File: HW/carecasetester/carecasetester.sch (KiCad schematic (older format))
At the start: 3 parts, among them J4 Conn_01x06_Male, SW1 SW_DIP_x02

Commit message: cc-tester v0.1 gerber filser genereret og 1. print bestilles
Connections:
- net testpoints/TP5: now reaches A1.21 (8)
- net RELAY/Relay_Driver: now reaches A1.29 (6)
- net testpoints/TP4: now reaches A1.30 (7)
- no-connect marks 21 -> 18
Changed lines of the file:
@@
 $Descr A4 11693 8268
 encoding utf-8
-Sheet 1 5
+Sheet 1 6
 Title ""
 Date ""
@@
 F5 "D4" I R 3400 2700 50
 F6 "D5" I R 3400 2775 50
-$EndSheet
-$Sheet
-S 7750 3100 700  375
+F7 "RELAY" I R 3400 2850 50
+$EndSheet
+$Sheet
+S 4150 3800 700  375
 U 5E3DBE35
 F0 "testpoints" 50
 F1 "testpoints.sch" 50
+F2 "TP4" I R 4850 3900 50
+F3 "TP5" I R 4850 4000 50
 $EndSheet
 Wire Wire Line
@@
 NoConn ~ 5275 2800
 NoConn ~ 5275 2900
-NoConn ~ 5275 3500
-NoConn ~ 5275 3600
-NoConn ~ 5275 3700
 NoConn ~ 5275 3800
 Wire Wire Line
@@
 Wire Wire Line
 	6125 2275 6125 1800
+$Sheet
+S 2575 3450 825  600
+U 5E3E43C1
+F0 "RELAY" 50
+F1 "relay.sch" 50
+F2 "Relay_Driver" I R 3400 3750 50
+F3 "RELAY" I R 3400 3575 50
+$EndSheet
+Wire Wire Line
+	3400 3575 3575 3575
+Wire Wire Line
+	3575 3575 3575 2850
+Wire Wire Line
+	3575 2850 3400 2850
+Wire Wire Line
+	3400 3750 3750 3750
+Wire Wire Line
+	3750 3750 3750 3500
+Wire Wire Line
+	3750 3500 5275 3500
+Wire Wire Line
+	4850 3900 4950 3900
+Wire Wire Line
+	4950 3900 4950 3600
+Wire Wire Line
+	4950 3600 5275 3600
+Wire Wire Line
+	4850 4000 5075 4000
+Wire Wire Line
+	5075 4000 5075 3700
+Wire Wire Line
+	5075 3700 5275 3700
 $EndSCHEMATC

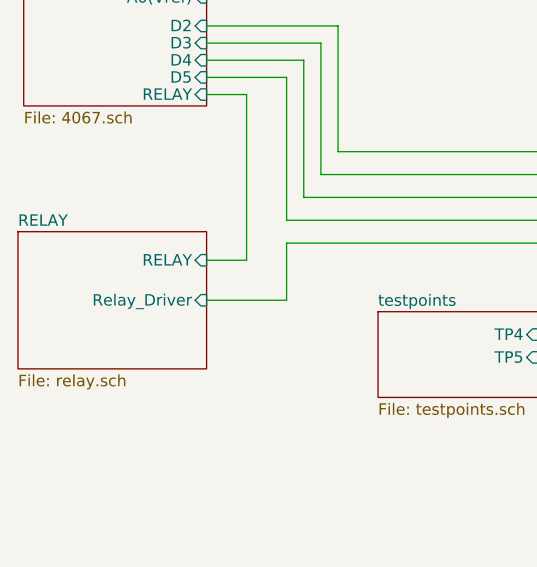
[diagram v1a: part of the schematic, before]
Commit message: Relay sheet filled and all pins matched.
starting changes made to pcb to fit schematic to the new pcb
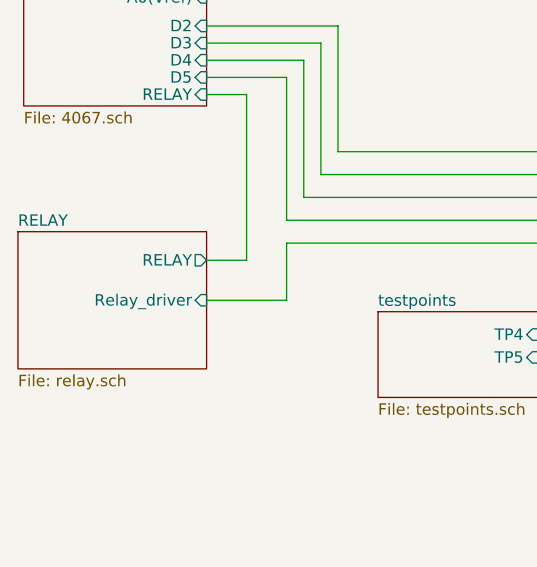
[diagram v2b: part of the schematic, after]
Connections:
- net RELAY/Relay_Driver renamed RELAY/Relay_driver
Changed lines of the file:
@@
 F0 "RELAY" 50
 F1 "relay.sch" 50
-F2 "Relay_Driver" I R 3400 3750 50
-F3 "RELAY" I R 3400 3575 50
+F2 "Relay_driver" I R 3400 3750 50
+F3 "RELAY" O R 3400 3575 50
 $EndSheet
 Wire Wire Line

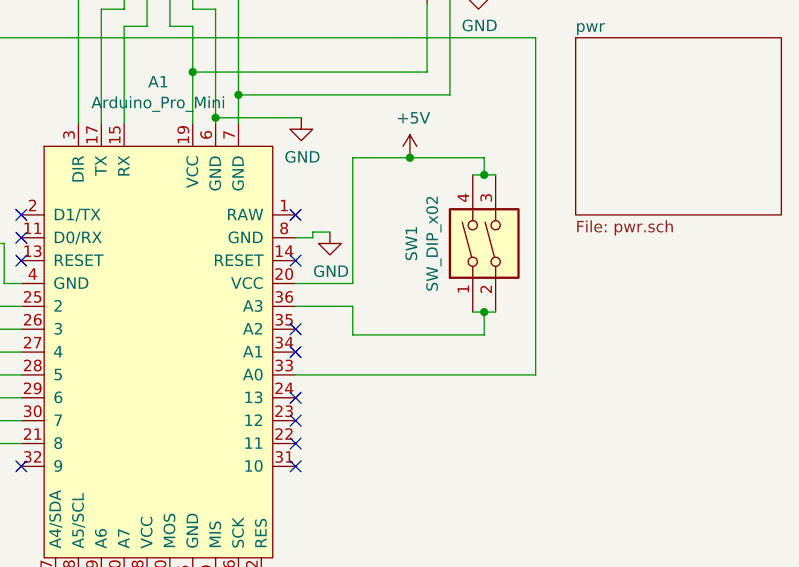
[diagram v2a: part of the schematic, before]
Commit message: First try to fit schematic to pcb (not imported footprints to pcb yet)
Schematic: All known components has gotten an updated footprint
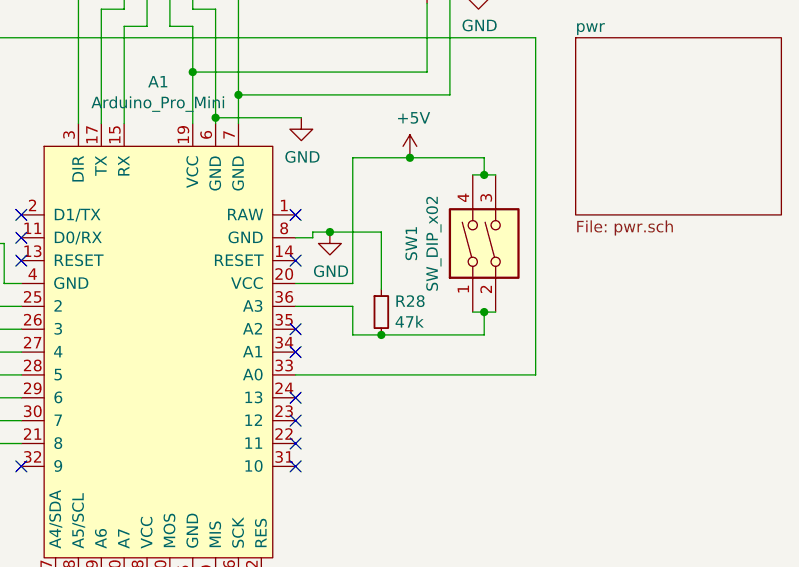
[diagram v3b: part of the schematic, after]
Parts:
- added R28: 47k, Resistor_SMD:R_0603_1608Metric_Pad1.05x0.95mm_HandSolder, symbol Device:R_Small
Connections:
- net GND: now also R28.1
- net at A1.36 (A3), SW1.1, SW1.2: now also R28.2
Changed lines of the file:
@@
 	6725 3100 6725 3225
 Wire Wire Line
-	6725 3225 7300 3225
+	6725 3225 6850 3225
 Wire Wire Line
 	7300 3225 7300 3125
@@
 Wire Wire Line
 	5075 3700 5275 3700
+$Comp
+L Device:R_Small R28
+U 1 1 5E870DAA
+P 6850 3125
+F 0 "R28" H 6909 3171 50  0000 L CNN
+F 1 "47k" H 6909 3080 50  0000 L CNN
+F 2 "Resistor_SMD:R_0603_1608Metric_Pad1.05x0.95mm_HandSolder" H 6850 3125 50  0001 C CNN
+F 3 "~" H 6850 3125 50  0001 C CNN
+	1    6850 3125
+	1    0    0    -1
+$EndComp
+Connection ~ 6850 3225
+Wire Wire Line
+	6850 3225 7300 3225
+Wire Wire Line
+	6850 3025 6850 2775
+Wire Wire Line
+	6850 2775 6625 2775
+Connection ~ 6625 2775
 $EndSCHEMATC

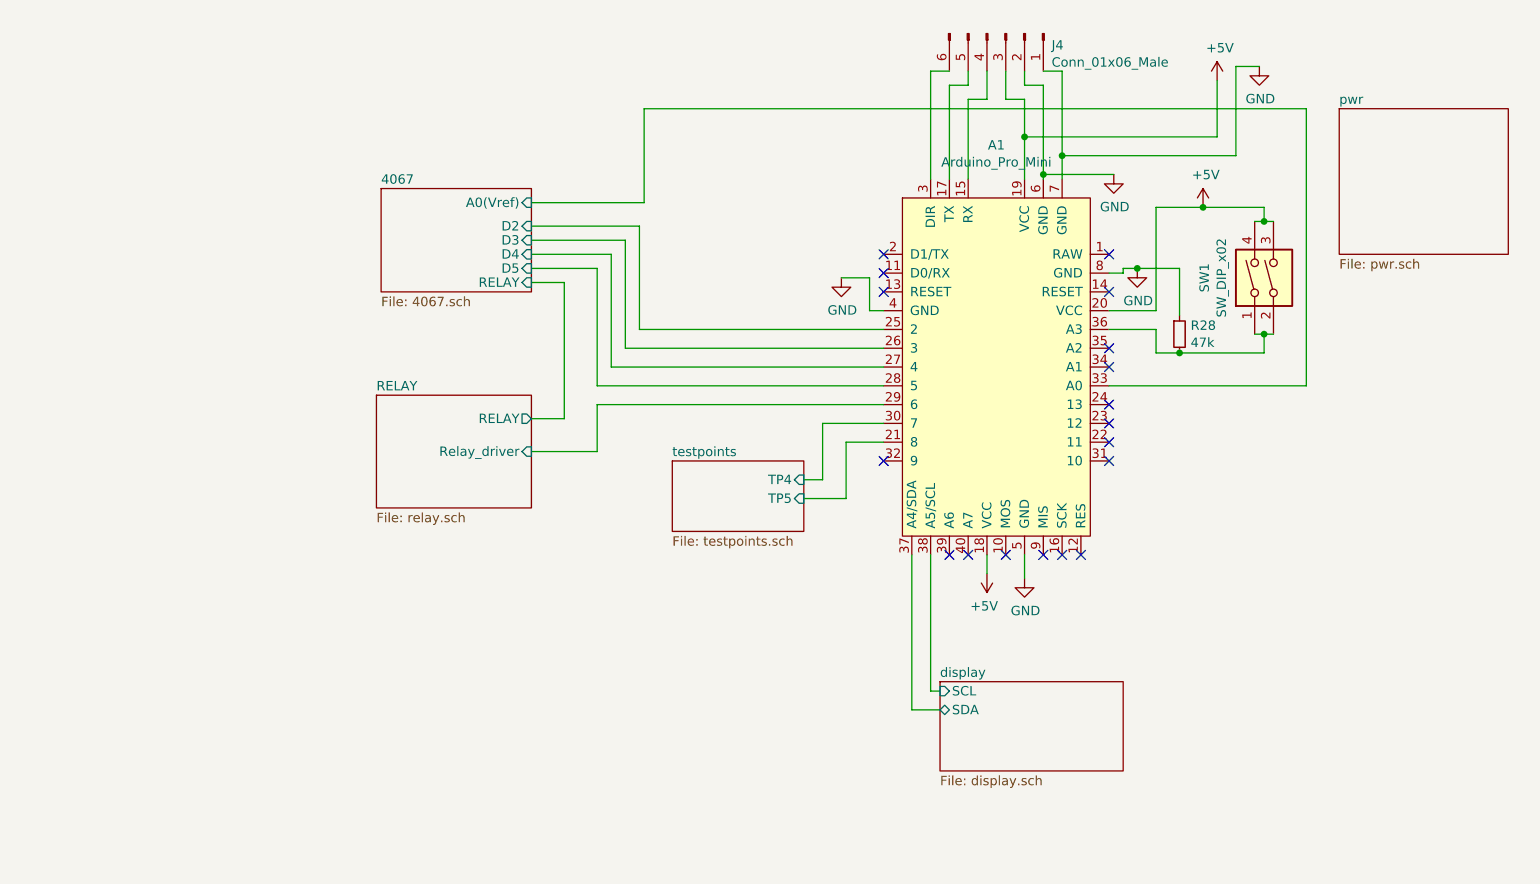
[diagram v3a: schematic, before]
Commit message: Gerbers and drillfiles made and ready to order
edge cuts file renamed to GML instaid of GM1
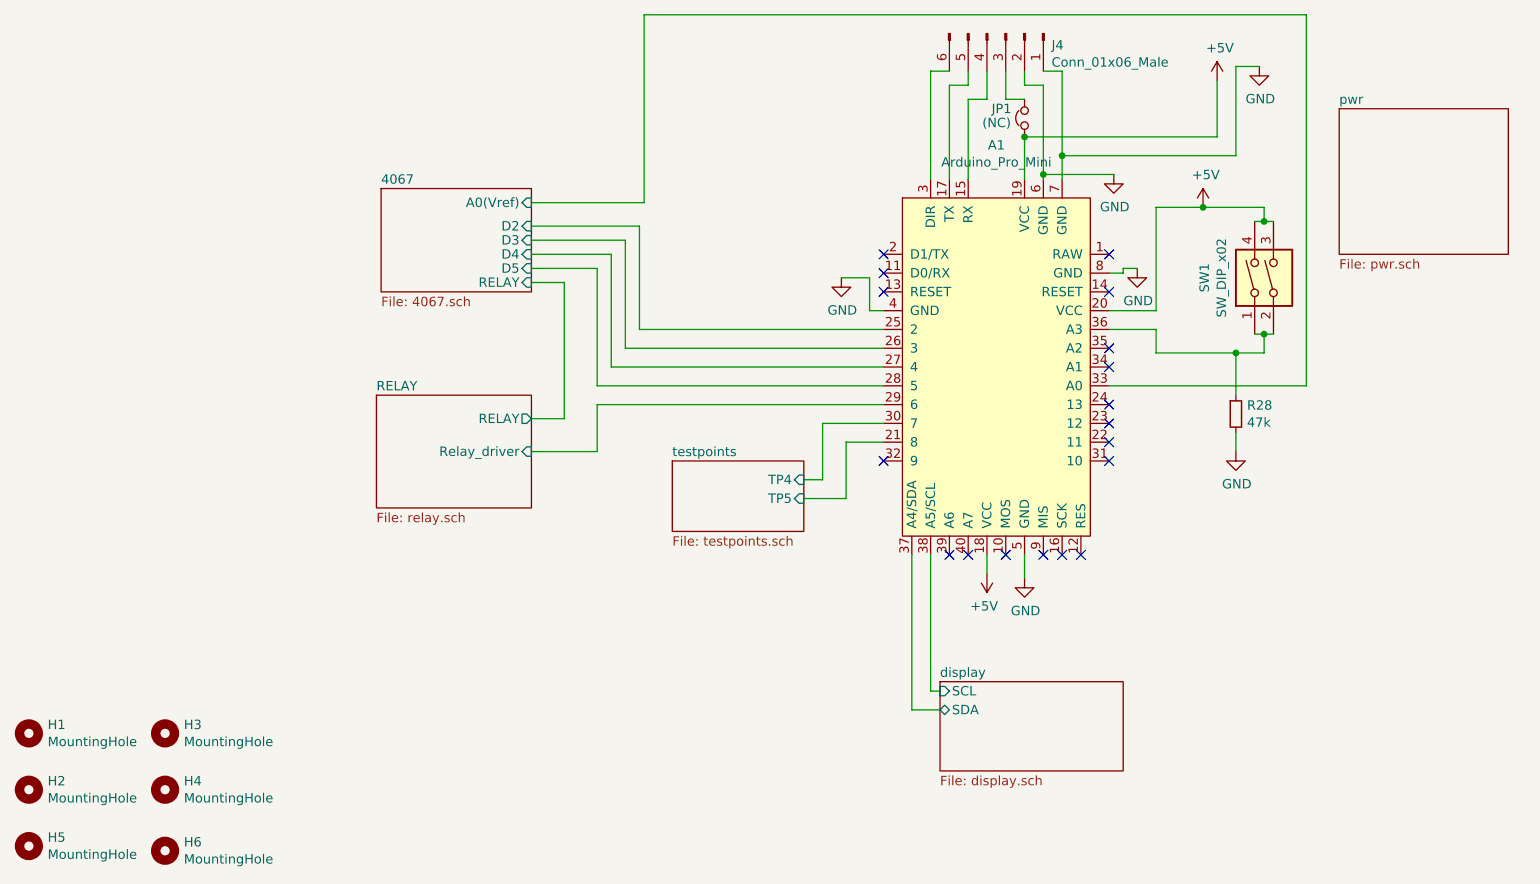
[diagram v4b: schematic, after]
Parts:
- added H1, H2, H3, H4, H5, H6: MountingHole, MountingHole:MountingHole_3.2mm_M3_ISO14580_Pad, symbol Mechanical:MountingHole
- added JP1: (NC), MM:Jumper_P2.54_Vertical_THT, symbol Device:Jumper_NC_Small
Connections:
- net +5V: now also JP1.1; no longer J4.3 (Pin_3)
- net GND: now also R28.2; no longer R28.1
- net at A1.36 (A3), SW1.1, SW1.2: now also R28.1; no longer R28.2
- new net: J4.3 (Pin_3), JP1.2
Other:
- moved on the sheet: R28
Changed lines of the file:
@@
 	3400 2425 4000 2425
 Wire Wire Line
-	4000 2425 4000 1925
-Wire Wire Line
-	7525 1925 7525 3400
+	4000 2425 4000 1425
+Wire Wire Line
+	7525 1425 7525 3400
 Wire Wire Line
 	7525 3400 6475 3400
@@
 	6725 3100 6725 3225
 Wire Wire Line
-	6725 3225 6850 3225
-Wire Wire Line
 	7300 3225 7300 3125
 Connection ~ 7300 3125
@@
 	6475 3100 6725 3100
 Wire Wire Line
-	4000 1925 7525 1925
+	4000 1425 7525 1425
 $Comp
 L Connector:Conn_01x06_Male J4
@@
 	6025 2300 6025 2075
 Wire Wire Line
-	6025 1875 5925 1875
-Wire Wire Line
-	5925 1875 5925 1725
-Wire Wire Line
 	6125 2300 6125 2275
 Wire Wire Line
@@
 Wire Wire Line
 	6225 1725 6125 1725
-Connection ~ 6025 2075
 NoConn ~ 5625 4300
 NoConn ~ 5725 4300
@@
 	1    0    0    -1
 $EndComp
-Wire Wire Line
-	6025 1875 6025 2075
 $Comp
 L power:+5V #PWR0110
@@
 L Device:R_Small R28
 U 1 1 5E870DAA
-P 6850 3125
-F 0 "R28" H 6909 3171 50  0000 L CNN
-F 1 "47k" H 6909 3080 50  0000 L CNN
-F 2 "Resistor_SMD:R_0603_1608Metric_Pad1.05x0.95mm_HandSolder" H 6850 3125 50  0001 C CNN
-F 3 "~" H 6850 3125 50  0001 C CNN
-	1    6850 3125
-	1    0    0    -1
-$EndComp
-Connection ~ 6850 3225
-Wire Wire Line
-	6850 3225 7300 3225
-Wire Wire Line
-	6850 3025 6850 2775
-Wire Wire Line
-	6850 2775 6625 2775
-Connection ~ 6625 2775
+P 7150 3550
+F 0 "R28" H 7209 3596 50  0000 L CNN
+F 1 "47k" H 7209 3505 50  0000 L CNN
+F 2 "Resistor_SMD:R_0603_1608Metric_Pad1.05x0.95mm_HandSolder" H 7150 3550 50  0001 C CNN
+F 3 "~" H 7150 3550 50  0001 C CNN
+	1    7150 3550
+	1    0    0    -1
+$EndComp
+$Comp
+L Mechanical:MountingHole H3
+U 1 1 5E86F871
+P 1450 5250
+F 0 "H3" H 1550 5296 50  0000 L CNN
+F 1 "MountingHole" H 1550 5205 50  0000 L CNN
+F 2 "MountingHole:MountingHole_3.2mm_M3_ISO14580_Pad" H 1450 5250 50  0001 C CNN
+F 3 "~" H 1450 5250 50  0001 C CNN
+	1    1450 5250
+	1    0    0    -1
+$EndComp
+$Comp
+L Mechanical:MountingHole H4
+U 1 1 5E870C6C
+P 1450 5550
+F 0 "H4" H 1550 5596 50  0000 L CNN
+F 1 "MountingHole" H 1550 5505 50  0000 L CNN
+F 2 "MountingHole:MountingHole_3.2mm_M3_ISO14580_Pad" H 1450 5550 50  0001 C CNN
+F 3 "~" H 1450 5550 50  0001 C CNN
+	1    1450 5550
+	1    0    0    -1
+$EndComp
+$Comp
+L Mechanical:MountingHole H1
+U 1 1 5E872C20
+P 725 5250
+F 0 "H1" H 825 5296 50  0000 L CNN
+F 1 "MountingHole" H 825 5205 50  0000 L CNN
+F 2 "MountingHole:MountingHole_3.2mm_M3_ISO14580_Pad" H 725 5250 50  0001 C CNN
+F 3 "~" H 725 5250 50  0001 C CNN
+	1    725  5250
+	1    0    0    -1
+$EndComp
+$Comp
+L Mechanical:MountingHole H2
+U 1 1 5E874A9F
+P 725 5550
+F 0 "H2" H 825 5596 50  0000 L CNN
+F 1 "MountingHole" H 825 5505 50  0000 L CNN
+F 2 "MountingHole:MountingHole_3.2mm_M3_ISO14580_Pad" H 725 5550 50  0001 C CNN
+F 3 "~" H 725 5550 50  0001 C CNN
+	1    725  5550
+	1    0    0    -1
+$EndComp
+$Comp
+L Mechanical:MountingHole H6
+U 1 1 5E877F41
+P 1450 5875
+F 0 "H6" H 1550 5921 50  0000 L CNN
+F 1 "MountingHole" H 1550 5830 50  0000 L CNN
+F 2 "MountingHole:MountingHole_3.2mm_M3_ISO14580_Pad" H 1450 5875 50  0001 C CNN
+F 3 "~" H 1450 5875 50  0001 C CNN
+	1    1450 5875
+	1    0    0    -1
+$EndComp
+$Comp
+L Mechanical:MountingHole H5
+U 1 1 5E877F47
+P 725 5850
+F 0 "H5" H 825 5896 50  0000 L CNN
+F 1 "MountingHole" H 825 5805 50  0000 L CNN
+F 2 "MountingHole:MountingHole_3.2mm_M3_ISO14580_Pad" H 725 5850 50  0001 C CNN
+F 3 "~" H 725 5850 50  0001 C CNN
+	1    725  5850
+	1    0    0    -1
+$EndComp
+$Comp
+L power:GND #PWR07
+U 1 1 5E872E95
+P 7150 3750
+F 0 "#PWR07" H 7150 3500 50  0001 C CNN
+F 1 "GND" H 7155 3577 50  0000 C CNN
+F 2 "" H 7150 3750 50  0001 C CNN
+F 3 "" H 7150 3750 50  0001 C CNN
+	1    7150 3750
+	1    0    0    -1
+$EndComp
+Wire Wire Line
+	6725 3225 7150 3225
+Wire Wire Line
+	7150 3750 7150 3650
+Wire Wire Line
+	7150 3450 7150 3225
+Connection ~ 7150 3225
+Wire Wire Line
+	7150 3225 7300 3225
+$Comp
+L Device:Jumper_NC_Small JP1
+U 1 1 5E88542A
+P 6025 1975
+F 0 "JP1" V 6075 2150 50  0000 R CNN
+F 1 "(NC)" V 6000 2200 50  0000 R CNN
+F 2 "MM:Jumper_P2.54_Vertical_THT" H 6025 1975 50  0001 C CNN
+F 3 "~" H 6025 1975 50  0001 C CNN
+	1    6025 1975
+	0    -1   -1   0
+$EndComp
+Connection ~ 6025 2075
+Wire Wire Line
+	6025 1875 5925 1875
+Wire Wire Line
+	5925 1875 5925 1725
 $EndSCHEMATC

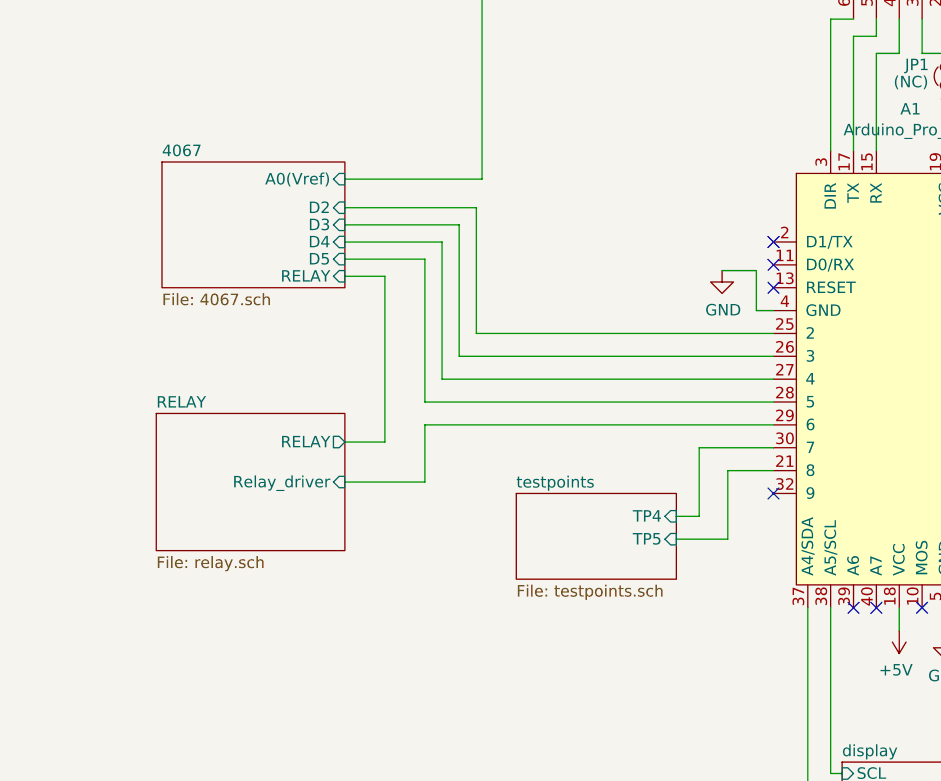
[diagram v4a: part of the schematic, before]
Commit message: V0.22 gerbers
2nd relay added and all should now be ready to order
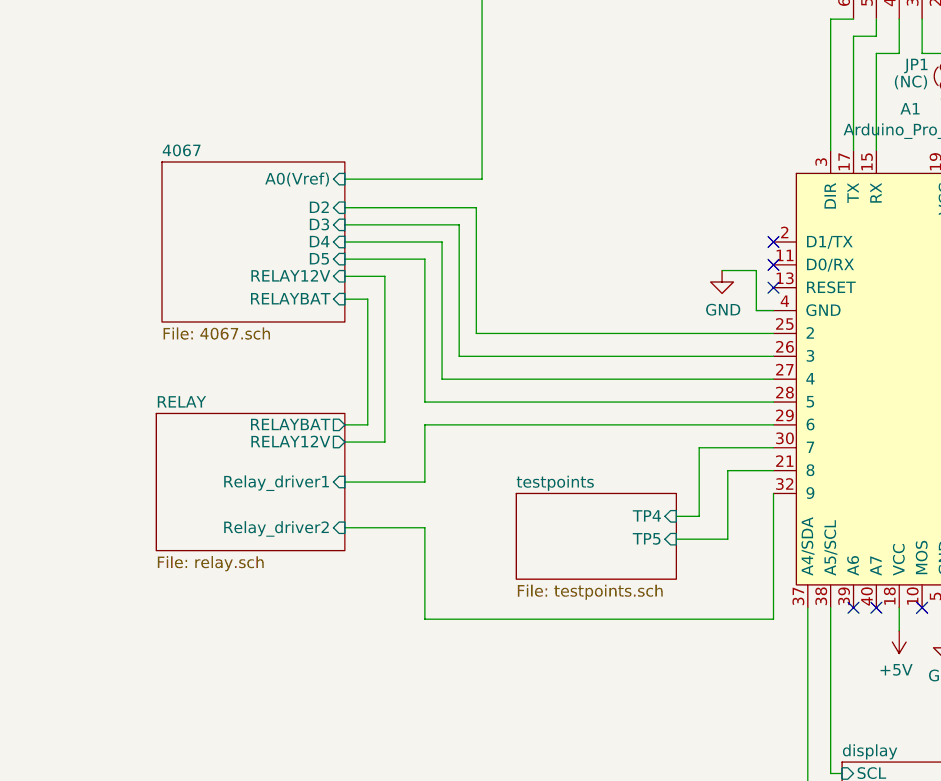
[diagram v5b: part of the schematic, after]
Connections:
- net RELAY/Relay_driver2: now reaches A1.32 (9)
- net RELAY/Relay_driver renamed RELAY/Relay_driver1
- no-connect marks 18 -> 17
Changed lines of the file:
@@
 	5525 5025 5575 5025
 $Sheet
-S 2600 2350 800  550
+S 2600 2350 800  700
 U 5E3BA6A3
 F0 "4067" 50
@@
 F5 "D4" I R 3400 2700 50
 F6 "D5" I R 3400 2775 50
-F7 "RELAY" I R 3400 2850 50
+F7 "RELAY12V" I R 3400 2850 50
+F8 "RELAYBAT" I R 3400 2950 50
 $EndSheet
 $Sheet
@@
 NoConn ~ 5275 2800
 NoConn ~ 5275 2900
-NoConn ~ 5275 3800
 Wire Wire Line
 	6725 2450 6975 2450
@@
 F0 "RELAY" 50
 F1 "relay.sch" 50
-F2 "Relay_driver" I R 3400 3750 50
-F3 "RELAY" O R 3400 3575 50
+F2 "Relay_driver1" I R 3400 3750 50
+F3 "RELAY12V" O R 3400 3575 50
+F4 "Relay_driver2" I R 3400 3950 50
+F5 "RELAYBAT" O R 3400 3500 50
 $EndSheet
 Wire Wire Line
@@
 Wire Wire Line
 	5925 1875 5925 1725
+Wire Wire Line
+	3400 2950 3500 2950
+Wire Wire Line
+	3500 2950 3500 3500
+Wire Wire Line
+	3500 3500 3400 3500
+Wire Wire Line
+	5275 3800 5275 4350
+Wire Wire Line
+	5275 4350 3750 4350
+Wire Wire Line
+	3750 4350 3750 3950
+Wire Wire Line
+	3750 3950 3400 3950
 $EndSCHEMATC
